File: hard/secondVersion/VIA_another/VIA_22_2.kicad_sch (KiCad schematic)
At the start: 12 parts, among them J1 port A, J2 port B, J3 myBus, Q1 2SB817, U1 W65C22, U3 74HC238

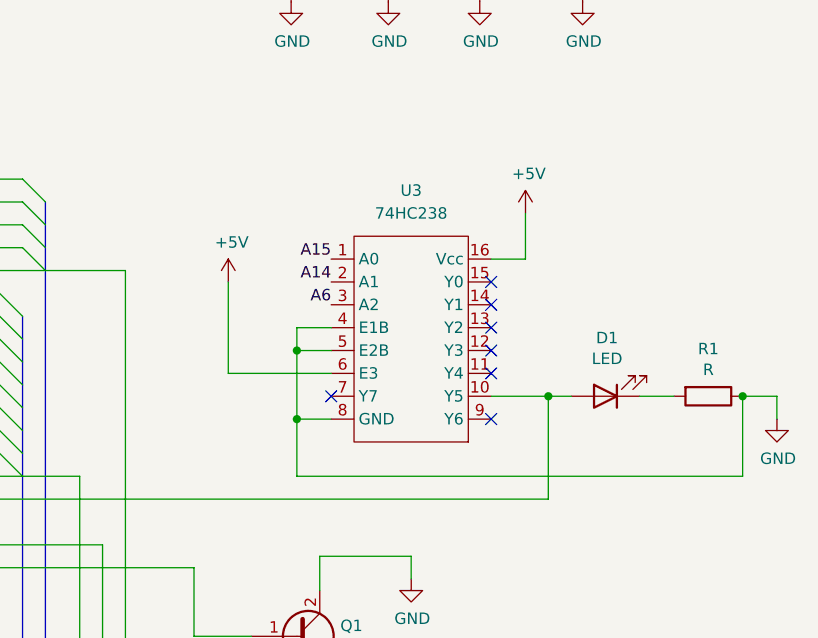
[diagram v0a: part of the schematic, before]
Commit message: VIA 2 schematcs
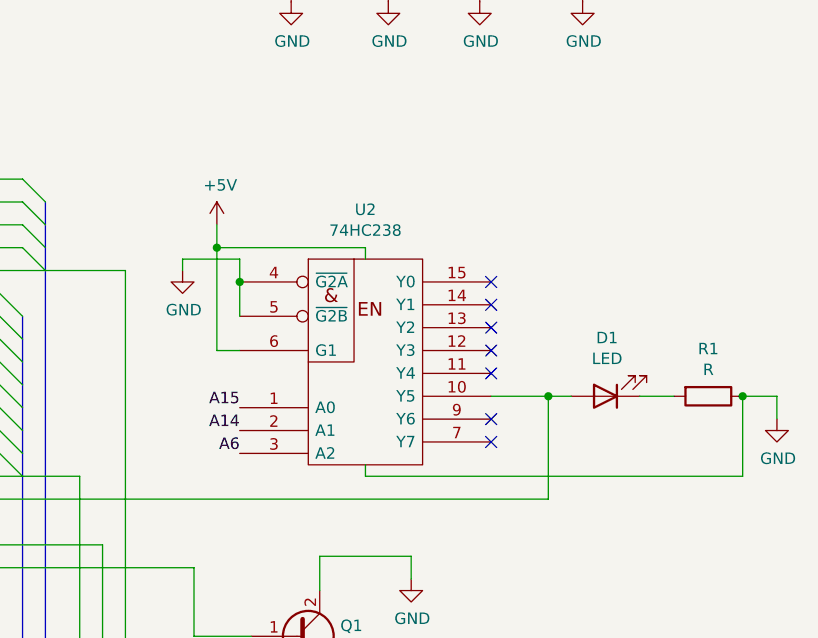
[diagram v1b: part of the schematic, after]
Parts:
- removed U3: 74HC238, symbol libFrom:74HC238
- added U2: 74HC238, Package_DIP:DIP-16_W7.62mm_Socket, symbol 74xx_IEEE:74HC238
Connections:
- net +5V: now also U2.16 (VCC), U2.6 (G1)
- net A14: now also U2.2 (A1)
- net A15: now also U2.1 (A0)
- net A6: now also U2.3 (A2)
- net GND: now also U2.4 (~{G2A}), U2.5 (~{G2B}), U2.8 (GND)
- net at D1.2 (A), U1.24 (CS1): now also U2.10 (Y5)
